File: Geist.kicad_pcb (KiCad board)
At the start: 2 copper layers, 80 x 80 mm, 46 parts, among them J1 USB_C_Receptacle_USB2.0_16P, J2 Conn_01x05, J3 Conn_01x03, J4 Conn_01x07, J5 Conn_01x05, J6 Conn_01x02, J7 Conn_01x02, J8 Conn_01x02, J9 Conn_01x02, U1 LM27762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

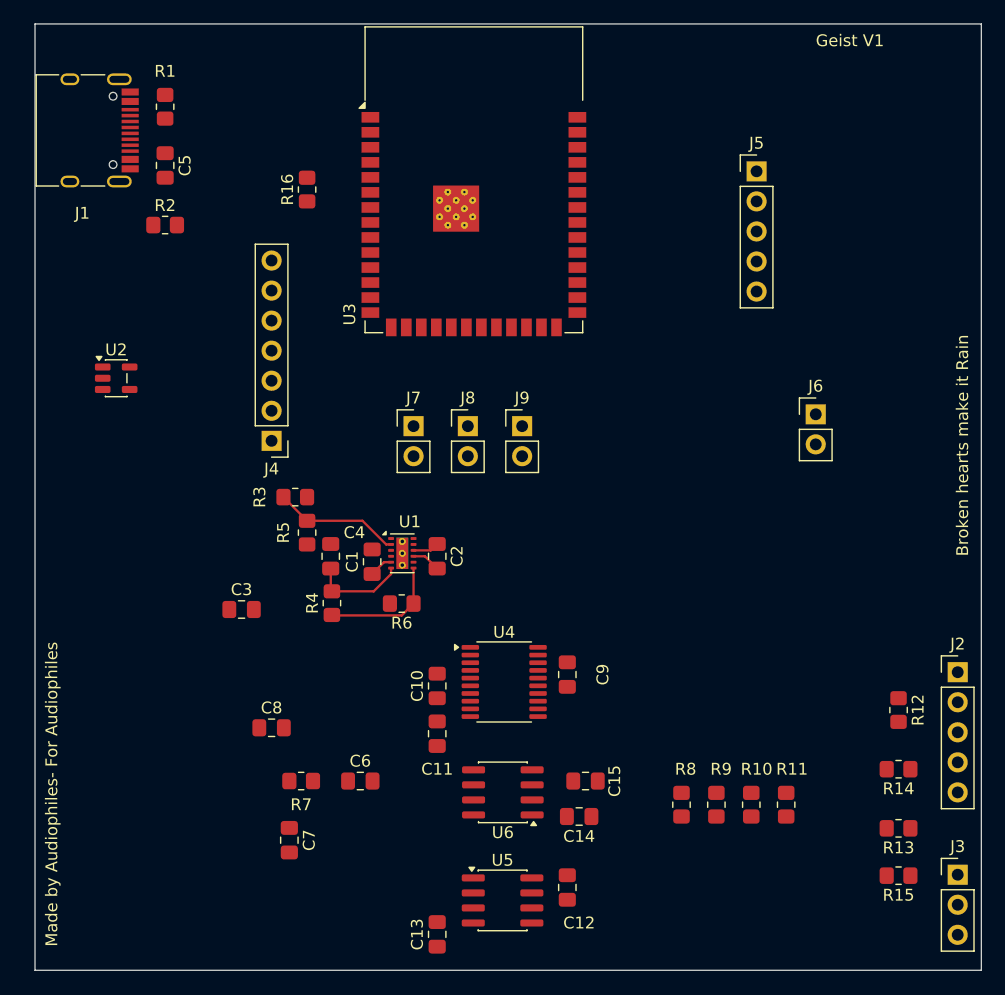
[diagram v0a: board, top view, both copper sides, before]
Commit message: GND pour
laid gnd pour on the pcb and adjusted some pins to suit better routing. Will work on chopping down DRC next.
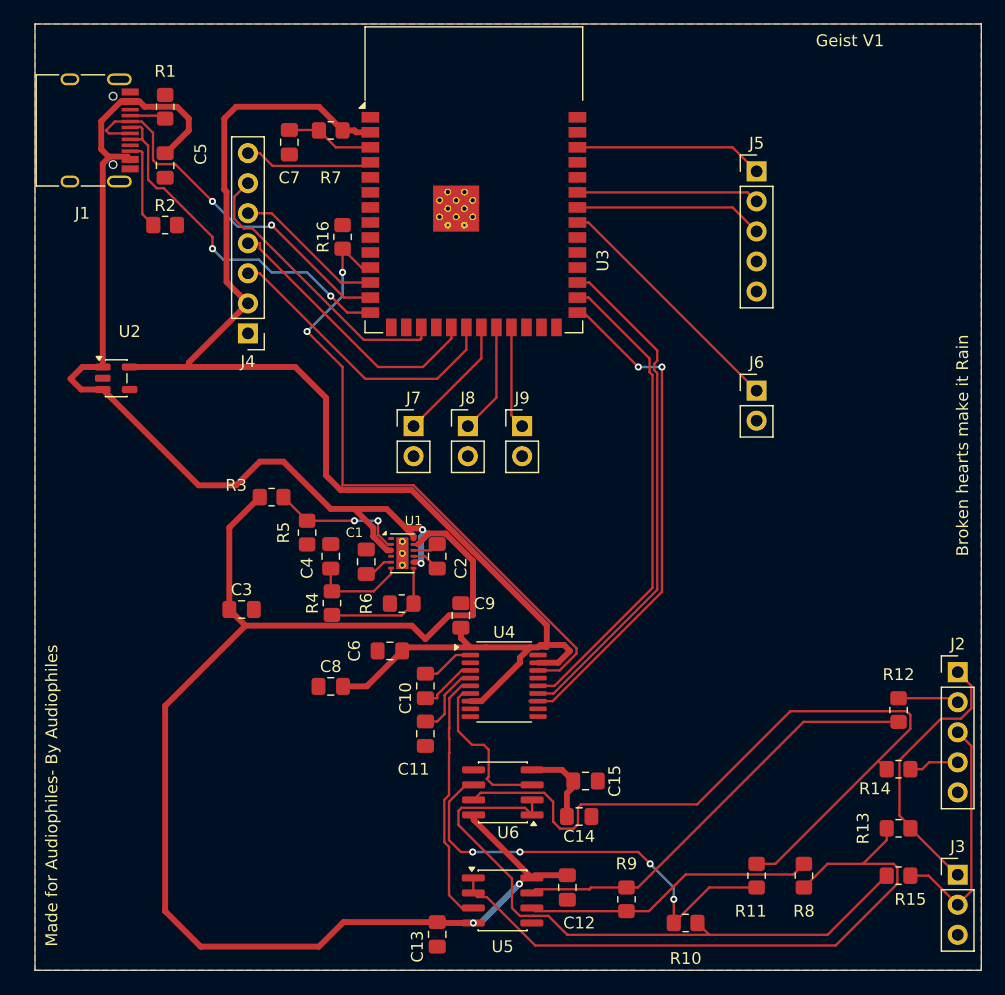
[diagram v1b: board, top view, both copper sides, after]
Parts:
- moved C7 59.0 mm to (131.5, 40.0)
- moved R7 55.1 mm to (135.0, 39.0)
- moved R8 12.0 mm to (175.0, 102.0)
- moved R10 11.4 mm to (165.0, 106.0), turned to 180 degrees
- moved C6 11.3 mm to (140.0, 83.0), turned to 180 degrees
- moved R9 11.0 mm to (160.0, 104.0), turned to 90 degrees
- moved C9 10.3 mm to (146.0, 80.0), turned to -90 degrees
- moved J4 9.30 mm to (128.0, 56.2)
- moved R11 6.50 mm to (171.0, 102.0), turned to 90 degrees
- moved C8 6.10 mm to (135.0, 86.0)
- moved J6 5.39 mm to (171.0, 61.0)
- moved R16 5.00 mm to (136.0, 48.0)
- moved R3 2.00 mm to (130.0, 70.0), turned to 0 degrees
- moved C10 1.00 mm to (143.0, 86.0)
- moved C11 1.00 mm to (143.0, 90.0)
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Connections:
- U3 pad 10: /BUTTON_NEXT -> unconnected-(U3-IO17-Pad10)
- U3 pad 18: /TFT_CS -> unconnected-(U3-IO10-Pad18)
- U3 pad 21: unconnected-(U3-IO13-Pad21) -> /BUTTON_PREV
- U3 pad 22: unconnected-(U3-IO14-Pad22) -> /BUTTON_PLAY
- U3 pad 23: /I2S_BCLK -> /BUTTON_NEXT
- U3 pad 27: unconnected-(U3-IO0-Pad27) -> /I2S_BCLK
- U3 pad 33: unconnected-(U3-IO40-Pad33) -> /TOGGLE_MODE
- U3 pad 34: unconnected-(U3-IO41-Pad34) -> /KNOB_SW
- U3 pad 35: unconnected-(U3-IO42-Pad35) -> /KNOB_B
- U3 pad 38: unconnected-(U3-IO2-Pad38) -> /KNOB_A
- U3 pad 4: /KNOB_A -> /TFT_CS
- U3 pad 5: /KNOB_B -> unconnected-(U3-IO5-Pad5)
- U3 pad 6: /KNOB_SW -> unconnected-(U3-IO6-Pad6)
- U3 pad 7: /TOGGLE_MODE -> unconnected-(U3-IO7-Pad7)
- U3 pad 8: /BUTTON_PREV -> unconnected-(U3-IO15-Pad8)
- U3 pad 9: /BUTTON_PLAY -> unconnected-(U3-IO16-Pad9)
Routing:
- net /3.3V: track 0.00 -> 120.9 mm
- net /+4.5V_Audio: track 0.00 -> 116.1 mm, vias 0 -> 2
- net +5V: track 0.00 -> 85.4 mm, vias 0 -> 2
- net /OUT_R-: track 0.00 -> 64.4 mm
- net /XSMT: track 0.00 -> 55.3 mm, vias 0 -> 2
- net /OUT_L+: track 0.00 -> 55.2 mm
- net /OUT_R+: track 0.00 -> 54.0 mm
- net /I2S_DATA: track 0.00 -> 43.3 mm
- net /I2S_BCLK: track 0.00 -> 43.1 mm, vias 0 -> 2
- net /I2S_LRCK: track 0.00 -> 40.8 mm
- net Net-(U6B--): track 0.00 -> 37.8 mm, vias 0 -> 4
- net /OUT_L-: track 0.00 -> 37.1 mm
- net /USB_D-: track 0.00 -> 32.5 mm, vias 0 -> 2
- net /USB_D+: track 0.00 -> 30.7 mm, vias 0 -> 2
- net /TFT_SCLK: track 0.00 -> 25.1 mm
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- added copper zone on B.Cu, net GND
- added copper zone on F.Cu, net GND
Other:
- board text added: "Buttons to be routed to bottom GPI/O"
- board text added: "Knob A, Knob B, Knob SW , Toggle mode to be routed to right hand side GPIO"
- board text added: "Made for Audiophiles- By Audiophiles"
- board text removed: "Made by Audiophiles- For Audiophiles"

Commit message: DRC fixes
further rectified DRC errors, now just need to add vias to thermal relief pads
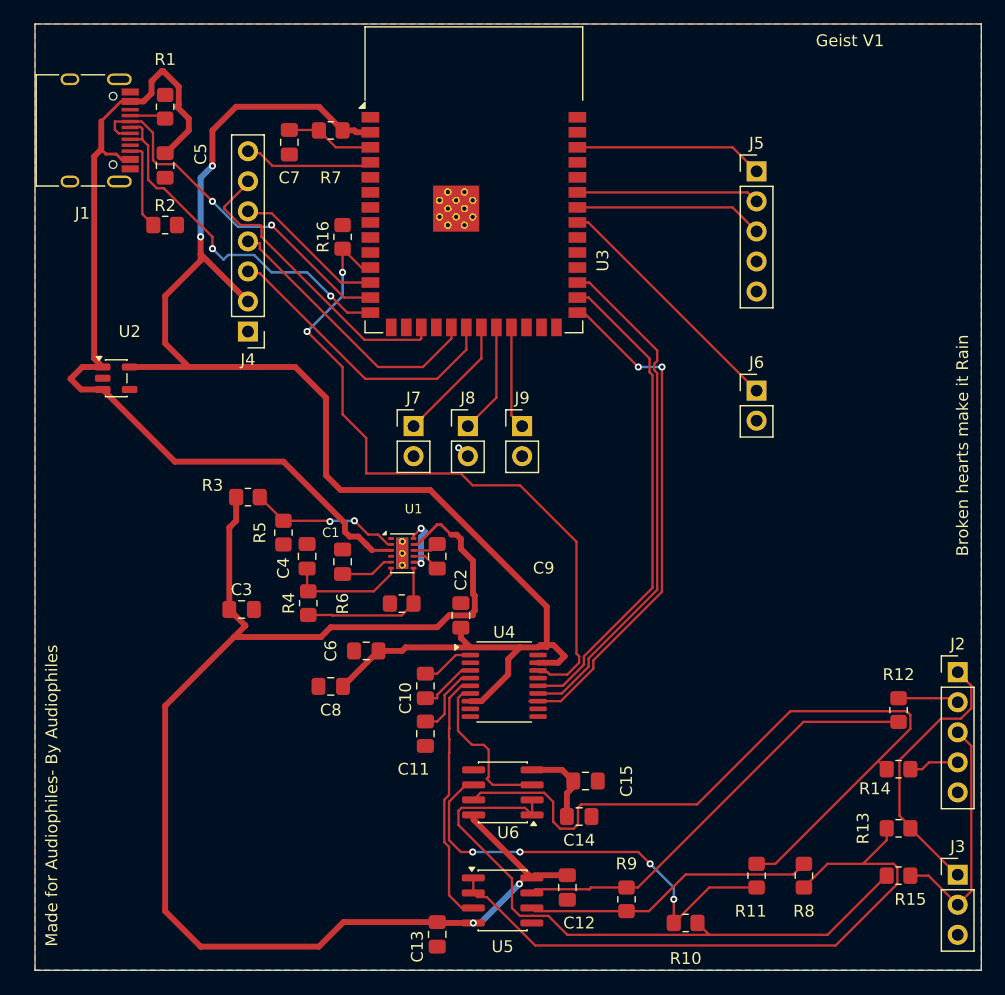
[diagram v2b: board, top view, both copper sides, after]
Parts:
- moved C1 2.00 mm to (136.0, 75.5)
- moved C4 2.00 mm to (133.0, 75.0)
- moved C6 2.00 mm to (138.0, 83.0)
- moved R3 2.00 mm to (128.0, 70.0)
- moved R4 2.00 mm to (133.1, 79.0)
- moved R5 2.00 mm to (131.0, 73.0)
- moved J4 0.16 mm to (128.0, 56.0)
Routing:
- net /3.3V: track 120.9 -> 127.0 mm, vias 0 -> 2
- net /XSMT: track 55.3 -> 59.8 mm
- net +5V: track 85.4 -> 82.3 mm
- net Net-(U1-CP): track 2.01 -> 4.51 mm
- net Net-(U1-FB-): track 10.3 -> 12.4 mm
- net Net-(U1-OUT-): track 8.07 -> 10.1 mm
- net /TFT_DC: track 24.5 -> 25.8 mm
- net Net-(U1-FB+): track 11.4 -> 12.5 mm
- net /USB_D-: track 32.5 -> 31.4 mm
- net GND: track 0.16 -> 1.22 mm, vias 0 -> 1
- net /+4.5V_Audio: track 116.1 -> 116.9 mm

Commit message: PCB Finished
FIxed all DRCs and made further design decisions like making usb c connector hang 1mm off the edge. Added mounting holes. PCB finished. Will add bitmap in next commit.
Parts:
- added REF**: MountingHole_3.2mm_M3, MountingHole:MountingHole_3.2mm_M3, F.Cu at (186.0, 106.0)
- added REF**: MountingHole_3.2mm_M3, MountingHole:MountingHole_3.2mm_M3, F.Cu at (114.0, 106.0)
- added REF**: MountingHole_3.2mm_M3, MountingHole:MountingHole_3.2mm_M3, F.Cu at (186.0, 34.0)
- added REF**: MountingHole_3.2mm_M3, MountingHole:MountingHole_3.2mm_M3, F.Cu at (114.0, 34.0)
- moved J2 7.49 mm to (187.0, 77.4)
- moved J3 7.49 mm to (187.0, 94.5)
- moved R12 7.49 mm to (182.0, 80.6)
- moved R13 7.49 mm to (182.0, 90.6)
- moved R14 7.49 mm to (182.0, 85.6)
- moved R15 7.49 mm to (182.0, 94.6)
- moved J1 4.12 mm to (113.0, 43.0)
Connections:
- U5 pad 4: /+4.5V_Audio -> /-4.5V_Audio
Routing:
- net GND: track 1.22 -> 102.2 mm, vias 1 -> 23
- net /-4.5V_Audio: track 7.09 -> 21.9 mm, vias 0 -> 2
- net /OUT_R-: track 64.4 -> 78.7 mm
- net /OUT_L+: track 55.2 -> 68.3 mm
- net /OUT_R+: track 54.0 -> 60.5 mm
- net +5V: track 82.3 -> 88.3 mm, vias 2 -> 3
- net Net-(J1-CC2): track 7.60 -> 4.02 mm
- net Net-(J1-CC1): track 3.06 -> 6.31 mm
- net /OUT_L-: track 37.1 -> 39.4 mm
- net Net-(J2-Pin_3): track 20.6 -> 22.8 mm
- net /USB_D+: track 31.0 -> 29.0 mm
- net /USB_D-: track 31.4 -> 29.5 mm
- net /+4.5V_Audio: track 116.9 -> 118.6 mm
- net Net-(J2-Pin_1): track 23.2 -> 24.7 mm
- net /DAC_LEFT: track 21.7 -> 22.9 mm
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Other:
- board text removed: "Buttons to be routed to bottom GPI/O"
- board text removed: "Knob A, Knob B, Knob SW , Toggle mode to be routed to right hand side GPIO"

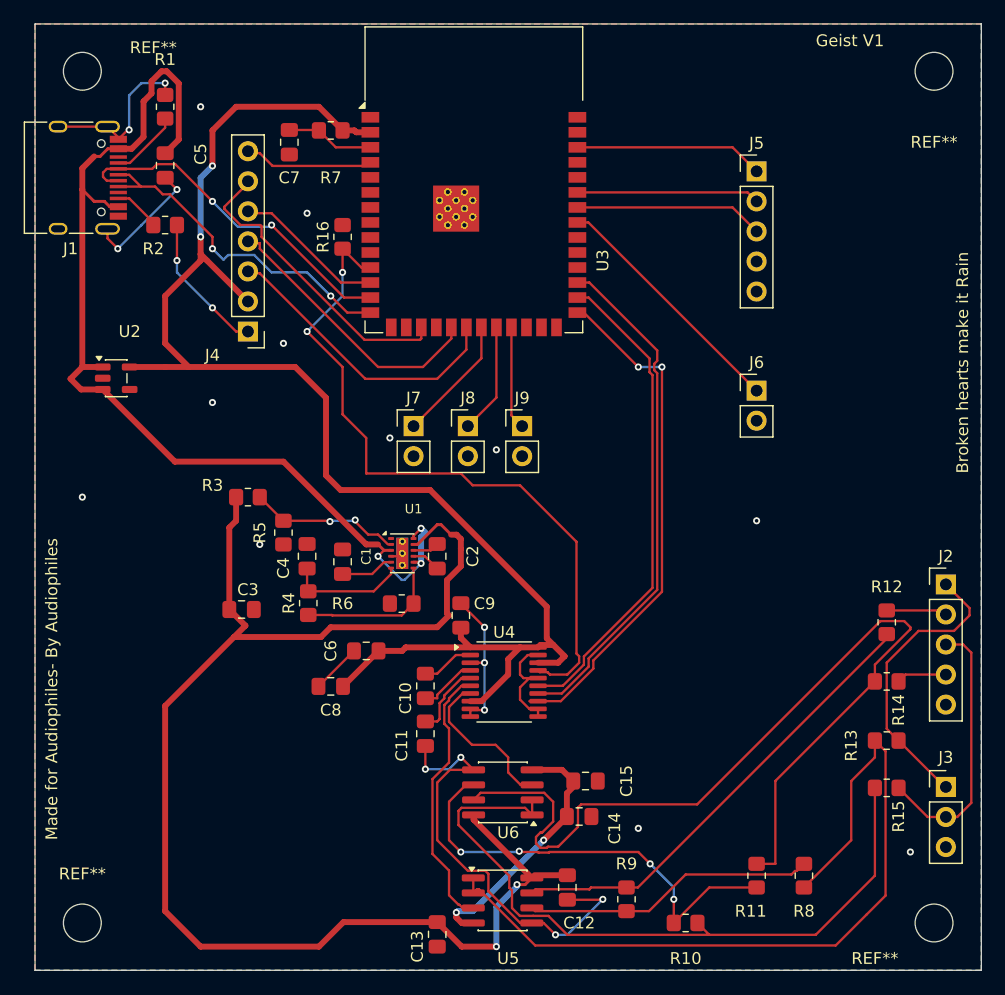
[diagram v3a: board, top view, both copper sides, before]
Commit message: Started enclosure +electric_to_air
started making enclosure in fusion 360 and board is fully finalised and rechecked multiple times. Added electric_to_air markdown file to explain the whole process start to finish.
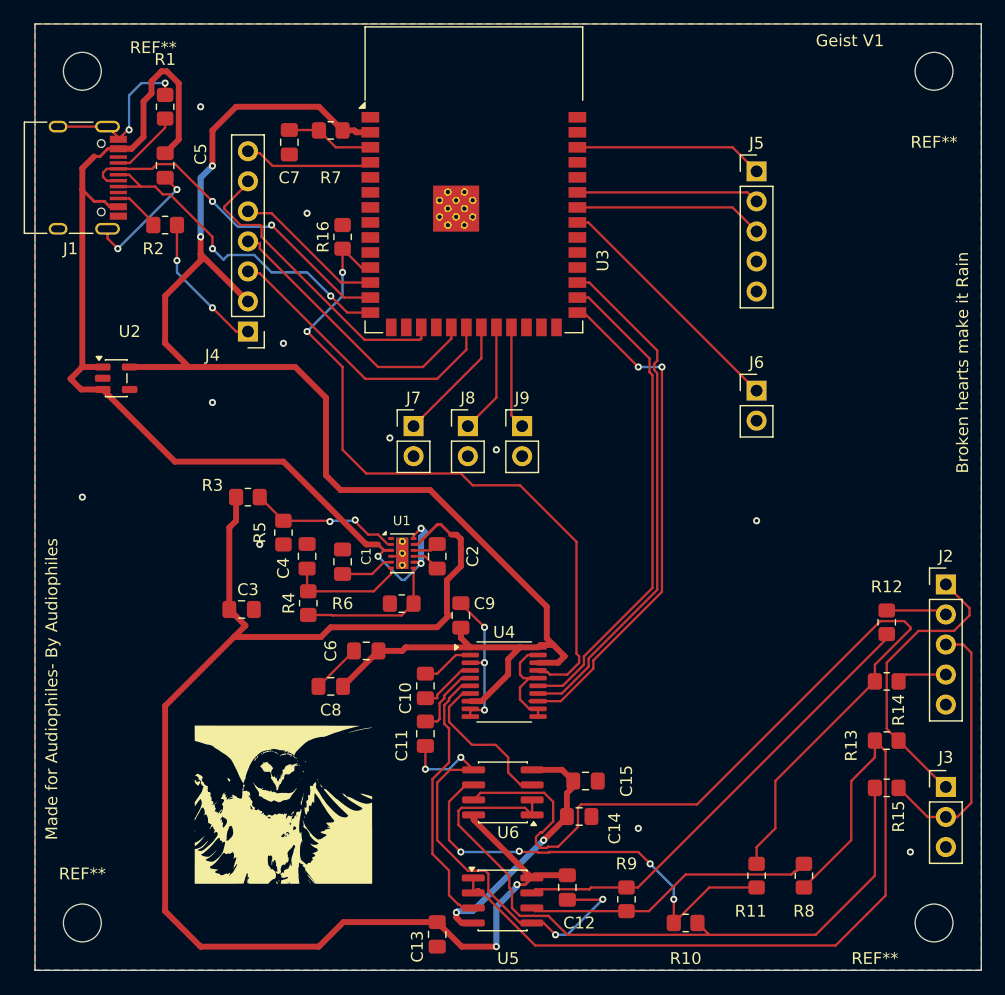
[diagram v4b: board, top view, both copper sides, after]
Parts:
- added G***: LOGO, Geist:owlv2, F.Cu at (131.0, 96.0)
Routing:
- net /OUT_R-: track 78.7 -> 77.8 mm
